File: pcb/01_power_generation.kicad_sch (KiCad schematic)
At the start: 0 parts

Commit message: Power conditioning and generation of +3V3, +A3V3, +5V and +12V from VBat
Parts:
- added C101, C102, C113: 100nF X7R 50V, FluxNode-FOC:C_0402_1005_DensityHigh, symbol Device:C
- added C103, C111: 22uF X7R 10V, FluxNode-FOC:C_0805_2012_DensityHigh, symbol Device:C
- added C104, C116: 2u2 X7R 100V, FluxNode-FOC:C_0805_2012_DensityHigh, symbol Device:C
- added C105, C106, C108, C109, C117: 2u2 100V, FluxNode-FOC:C_0805_2012_DensityHigh, symbol Device:C
- added C107: 100nF 100V, FluxNode-FOC:C_0603_1608_DensityHigh, symbol Device:C
- added C110: 10u 25V, FluxNode-FOC:C_0805_2012_DensityHigh, symbol Device:C
- added C112: 1uF X7R 10V, FluxNode-FOC:C_0402_1005_DensityHigh, symbol Device:C
- added C114, C115: 15uF 25V, FluxNode-FOC:C_1210_3225_DensityHigh, symbol Device:C
- added C118, C119: 4u7 100V, FluxNode-FOC:C_1206_3216_DensityHigh, symbol Device:C
- added C120, C121: 220n 100V, FluxNode-FOC:C_0603_1608_DensityHigh, symbol Device:C
- added C122: 1u 25V, FluxNode-FOC:C_0603_1608_DensityHigh, symbol Device:C
- added C123: 10n 100V, FluxNode-FOC:C_0402_1005_DensityHigh, symbol Device:C
- added C124: 4.7u 16V, FluxNode-FOC:C_0603_1608_DensityHigh, symbol Device:C
- added C125: 1u X7R 10V, FluxNode-FOC:C_0402_1005_DensityHigh, symbol Device:C
- added C126, C127, C128, C129, C130, C131, C132, C133, C134, C135, C136, C137, C138, C139, C140, C141, C142, C143, C144, C145, C146, C147, C148, C149, C150, C151, C152, C153, C154, C155, C156, C157, C158, C159, C160, C161, C162, C163, C164, C165, C166, C167, C168, C169, C170, C171, C172, C173: 4.7u 100V, FluxNode-FOC:C_1206_3216_DensityHigh, symbol Device:C
- added FB101, FB102, FB103: 1k @ 100MHz, FluxNode-FOC:R_0805_2012_DensityHigh, symbol Device:FerriteBead
- added L101, L103: 22uH 830mA 360mOhms, FluxNode-FOC:L_Coilcraft_LPS4018, symbol Device:L
- added L102: 2.2uH 1,2A 100mOhms, FluxNode-FOC:L_Coilcraft_LPS3314, symbol Device:L
- added NT101: VOS_3V3, symbol Device:NetTie_2
- added NT102: FB_5V, symbol Device:NetTie_2
- added NT103: FB_12V, symbol Device:NetTie_2
- added R101: 10k 1% 50V, FluxNode-FOC:R_0402_1005_DensityHigh, symbol Device:R
- added R102: 0R, FluxNode-FOC:R_0402_1005_DensityHigh, symbol Device:R
- added R103: 100k 1% 50V, FluxNode-FOC:R_0402_1005_DensityHigh, symbol Device:R
- added R104: 9.09k 1% 50V, FluxNode-FOC:R_0402_1005_DensityHigh, symbol Device:R
- added U101: TPS62172DSG, Package_SON:WSON-8-1EP_2x2mm_P0.5mm_EP0.9x1.6mm_ThermalVias, symbol Regulator_Switching:TPS62172DSG
- added U102: LMR36506MSC5RPERQ1, FluxNode-FOC:LMR36503, symbol FluxNode-FOC:LMR36506MSC5RPERQ1
- added U103: LP2992IM5-3.3/NOPB, Package_TO_SOT_SMD:SOT-23-5, symbol FluxNode-FOC:LP2992IM5-3.3/NOPB
- added U104: LMR36006FSCQ, FluxNode-FOC:LMR36006, symbol FluxNode-FOC:LMR36006FSCQ
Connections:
- new net: C112.1, R102.1, U102.1 (MODE/SYNC)
- new net: NT103.1, R103.1
- new net: C125.1, U104.5 (VCC)
- new net +12V: C114.1, C115.1, L103.2, NT103.2
- new net +3V3: C111.1, L102.2, NT101.2
- new net +5V: C102.1, C103.1, C108.1, C122.1, FB102.1, L101.2, NT102.2, R101.1, U103.1 (VIN)
- new net +A3V3: C124.1, U103.5 (VOUT)
- new net +VBAT: C104.1, C116.1, C126.1, C127.1, C128.1, C129.1, C130.1, C131.1, C132.1, C133.1, C134.1, C135.1, C136.1, C137.1, C138.1, C139.1, C140.1, C141.1, C142.1, C143.1, C144.1, C145.1, C146.1, C147.1, C148.1, C149.1, C150.1, C151.1, C152.1, C153.1, C154.1, C155.1, C156.1, C157.1, C158.1, C159.1, C160.1, C161.1, C162.1, C163.1, C164.1, C165.1, C166.1, C167.1, C168.1, C169.1, C170.1, C171.1, C172.1, C173.1, FB101.1, FB103.1
- new net 5V_VIN_3V3: C109.1, C110.1, FB102.2, U101.2 (VIN)
- new net ADJ_A3V3: C123.1, U103.4 (ADJ)
- new net BOOT_12V: C113.2, U104.4 (BOOT)
- new net BOOT_5V: C101.2, U102.6 (BOOT)
- new net FB_5V: NT102.1, U102.8 (FB)
- new net FB_DIV_12V: R103.2, R104.1, U104.7 (FB)
- new net F_VIN_12V: C117.1, C118.1, C119.1, C120.1, C121.1, FB103.2, U104.10 (VIN), U104.2 (VIN), U104.9 (EN)
- new net F_VIN_5V: C105.1, C106.1, C107.1, FB101.2, U102.3 (EN/UVLO), U102.4 (VIN)
- new net GND: C102.2, C103.2, C104.2, C105.2, C106.2, C107.2, C108.2, C109.2, C110.2, C111.2, C112.2, C114.2, C115.2, C116.2, C117.2, C118.2, C119.2, C120.2, C121.2, C122.2, C123.2, C124.2, C125.2, C126.2, C127.2, C128.2, C129.2, C130.2, C131.2, C132.2, C133.2, C134.2, C135.2, C136.2, C137.2, C138.2, C139.2, C140.2, C141.2, C142.2, C143.2, C144.2, C145.2, C146.2, C147.2, C148.2, C149.2, C150.2, C151.2, C152.2, C153.2, C154.2, C155.2, C156.2, C157.2, C158.2, C159.2, C160.2, C161.2, C162.2, C163.2, C164.2, C165.2, C166.2, C167.2, C168.2, C169.2, C170.2, C171.2, C172.2, C173.2, R102.2, R104.2, U101.1 (PGND), U101.4 (AGND), U101.5 (FB), U101.9 (PAD), U102.9 (GND), U103.2 (GND), U104.1 (PGND), U104.11 (PGND), U104.6 (AGND)
- new net PG_12V: U104.8 (PG)
- new net PG_3V3: U101.8 (PG)
- new net PG_5V: R101.2, U101.3 (EN), U102.2 (PGOOD), U103.3 (ON/~{OFF})
- new net SW_12V: C113.1, L103.1, U104.12 (SW), U104.3 (NC)
- new net SW_3V3: L102.1, U101.7 (SW)
- new net SW_5V: C101.1, L101.1, U102.5 (SW)
- new net VOS_3V3: NT101.1, U101.6 (VOS)
- no-connect marks 0 -> 2

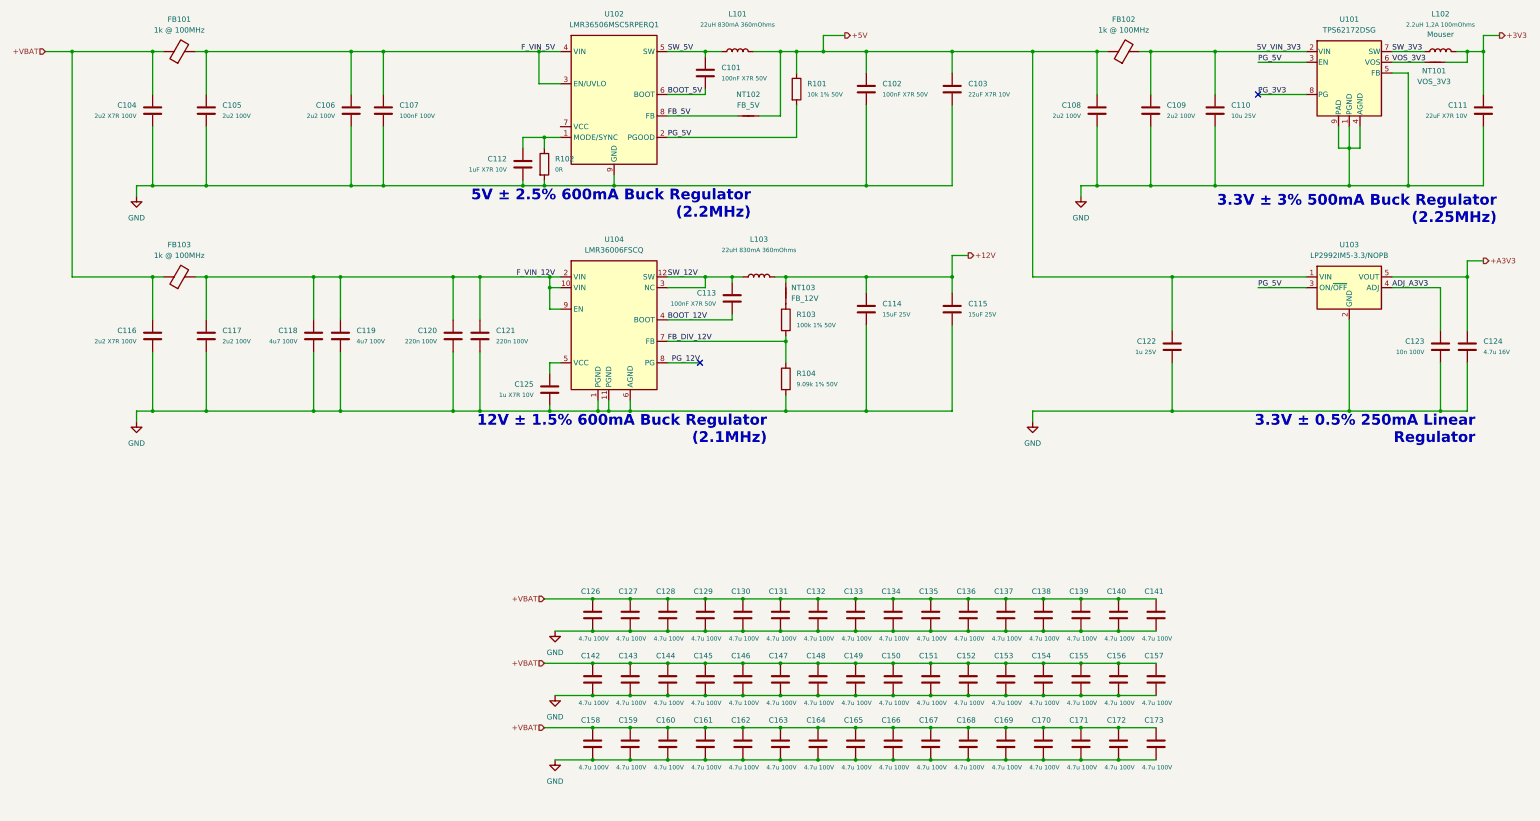
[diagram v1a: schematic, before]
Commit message: Unified all different LCSC part numbers of the same exact components to just one variant
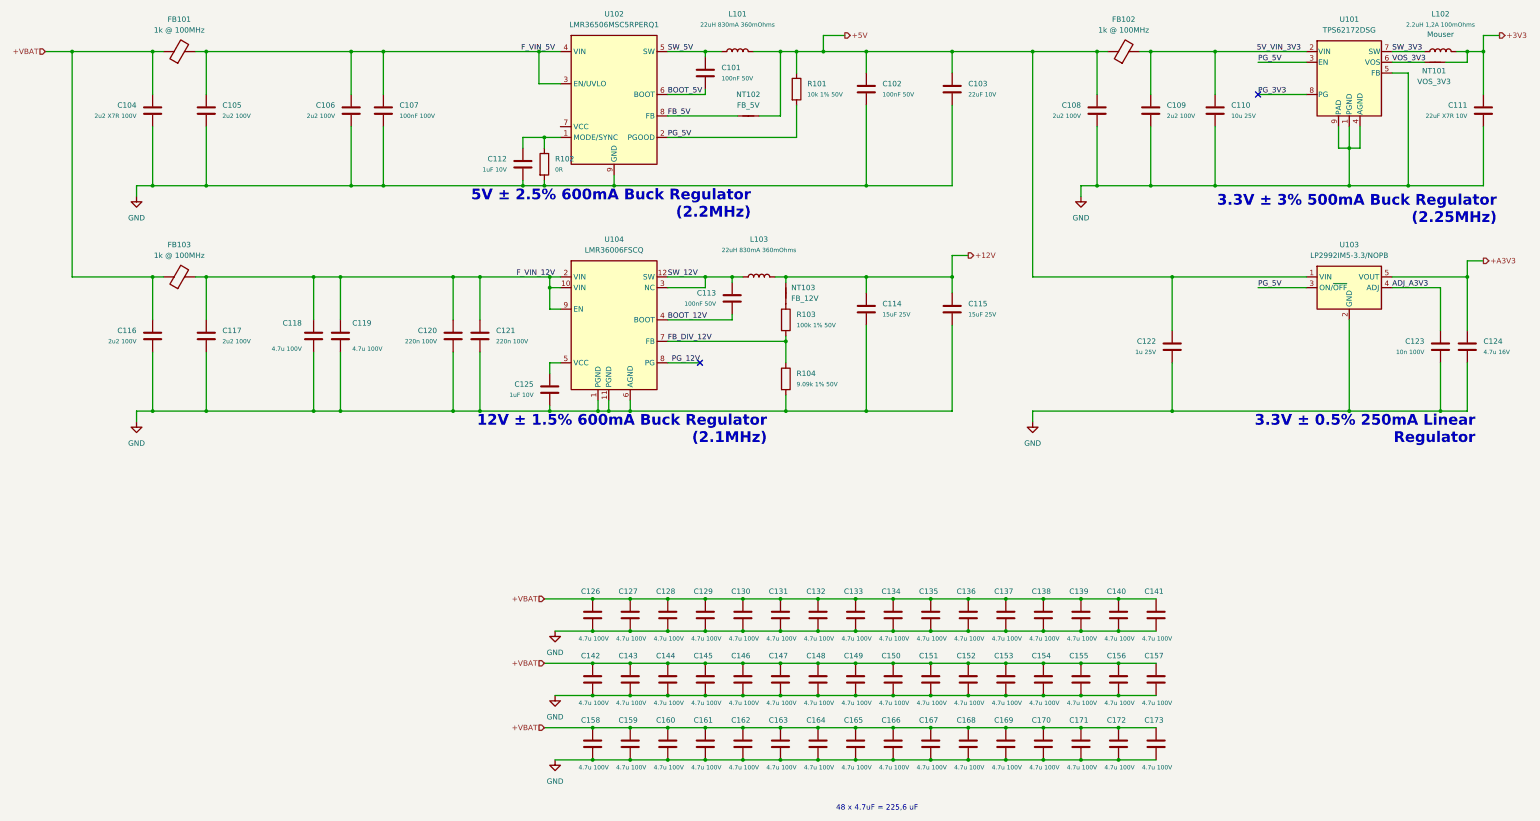
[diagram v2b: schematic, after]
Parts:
- C101, C102, C113: value 100nF X7R 50V -> 100nF 50V
- C103: value 22uF X7R 10V -> 22uF 10V
- C112: value 1uF X7R 10V -> 1uF 10V
- C116: value 2u2 X7R 100V -> 2u2 100V
- C118, C119: value 4u7 100V -> 4.7u 100V; LCSC C47117455 -> C33546020; MPN CIA1206X7R475K101NT -> HHV1206R7475M101NSPJ
- C125: value 1u X7R 10V -> 1uF 10V; LCSC C3858658 -> C47325373; MPN GRM155Z71A105KE01J -> TCC0402X7R105K100AT
- R104: LCSC C854467 -> C3013189; MPN RT0402FRE079K09L -> FRC0402F9091TS
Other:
- note added: "48 x 4.7uF = 225,6 uF"
- company: (none) -> PhiMai

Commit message: Some minor changes to the annotations
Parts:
- renumbered C104 to C1, C109 to C10, C110 to C11, C111 to C12, C116 to C13, C117 to C14, C118 to C15, C119 to C16, C120 to C17, C121 to C18, C125 to C19, C105 to C2, C113 to C20, C114 to C21, C115 to C22, C122 to C23, C123 to C24, C124 to C25, C126 to C26, C127 to C27, C128 to C28, C129 to C29, C106 to C3, C130 to C30, C131 to C31, C132 to C32, C133 to C33, C134 to C34, C135 to C35, C136 to C36, C137 to C37, C138 to C38, C139 to C39, C107 to C4, C140 to C40, C141 to C41, C142 to C42, C143 to C43, C144 to C44, C145 to C45, C146 to C46, C147 to C47, C148 to C48, C149 to C49, C112 to C5, C150 to C50, C151 to C51, C152 to C52, C153 to C53, C154 to C54, C155 to C55, C156 to C56, C157 to C57, C158 to C58, C159 to C59, C101 to C6, C160 to C60, C161 to C61, C162 to C62, C163 to C63, C164 to C64, C165 to C65, C166 to C66, C167 to C67, C168 to C68, C169 to C69, C102 to C7, C170 to C70, C171 to C71, C172 to C72, C173 to C73, C103 to C8, C108 to C9, FB101 to FB1, FB102 to FB2, FB103 to FB3, L101 to L1, L102 to L2, L103 to L3, NT101 to NT1, NT102 to NT2, NT103 to NT3, R102 to R1, R101 to R2, R103 to R3, R104 to R4, U101 to U1, U102 to U2, U103 to U3, U104 to U4
